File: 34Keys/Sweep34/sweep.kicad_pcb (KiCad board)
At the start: 2 copper layers, 110 x 88.6 mm, 21 parts, among them J1 MJ-4PP-9, SW10 SW_PUSH, SW11 SW_PUSH, SW12 SW_PUSH, SW14 SW_PUSH, SW15 SW_PUSH, SW16 SW_PUSH, SW17 SW_PUSH, SW18 SW_PUSH, SW2 SW_PUSH, SW20 SW_PUSH, SW21 SW_PUSH, SW3 SW_PUSH, SW4 SW_PUSH, SW5 SW_PUSH, SW6 SW_PUSH, SW8 SW_PUSH, SW9 SW_PUSH, U1 ProMicro

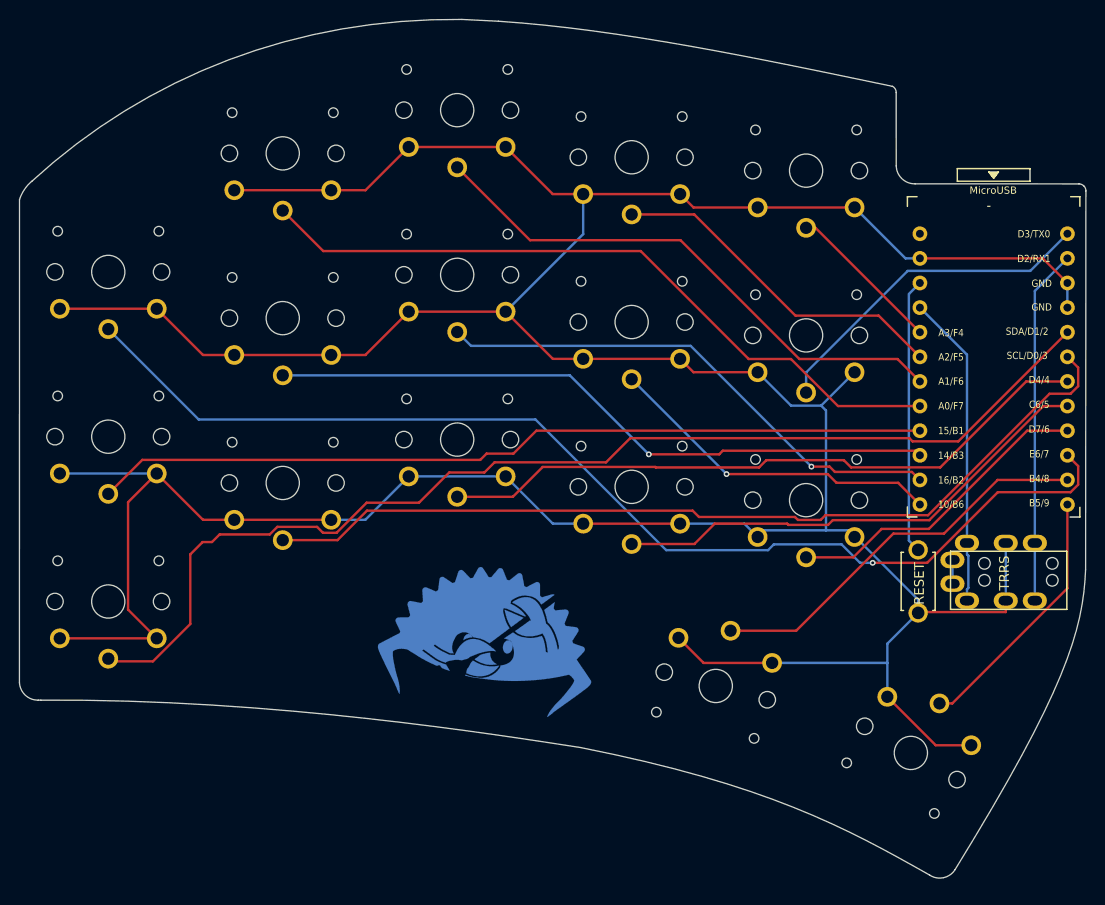
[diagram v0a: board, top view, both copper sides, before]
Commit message: fix promicro footprint, centre ferris move thumbs.
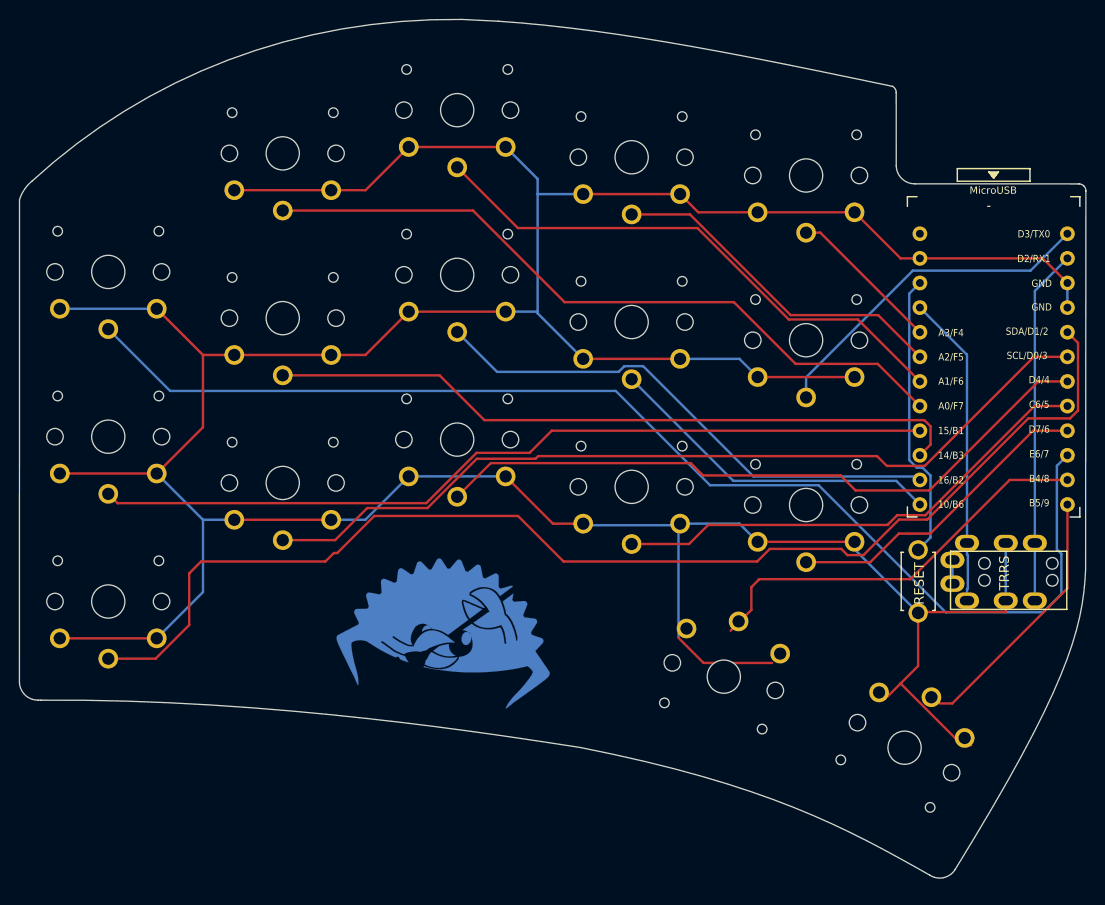
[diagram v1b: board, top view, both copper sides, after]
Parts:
- moved G*** 4.36 mm to (80.1, 80.4)
- moved SW20 1.27 mm to (107.5, 84.1)
- moved SW21 0.85 mm to (126.2, 91.5), turned to 332 degrees
- moved SW12 0.50 mm to (116.0, 49.4)
- moved SW18 0.50 mm to (116.0, 66.4)
- moved SW6 0.50 mm to (116.0, 32.4)
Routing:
- net GND: track 404.5 -> 393.6 mm
- net row3: track 117.4 -> 126.2 mm, vias 1 -> 0
- net SDA: track 118.1 -> 126.7 mm
- net SCL: track 92.9 -> 89.6 mm
- net col5: track 69.5 -> 72.5 mm, vias 1 -> 0
- net row0: track 68.6 -> 70.2 mm
- net Net-(U1-Pad11): track 41.2 -> 42.6 mm
- net reset: track 28.4 -> 29.8 mm
- net col4: track 86.4 -> 87.2 mm
- net Net-(U1-Pad14): track 54.1 -> 54.6 mm, vias 1 -> 0
- net Net-(U1-Pad13): vias 1 -> 0

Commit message: let's get these thumbs something like ferris
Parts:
- moved SW20 1.74 mm to (109.0, 85.1)
- moved SW21 1.72 mm to (127.6, 92.4)
- moved G*** 0.28 mm to (79.8, 80.3)
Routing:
- net GND: track 393.6 -> 396.0 mm
- net Net-(U1-Pad11): track 42.6 -> 41.7 mm
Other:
- board size 110 x 88.6 mm -> 110 x 89.3 mm
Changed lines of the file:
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@@
   )
   (module Kailh:SW_PG1350_reversible_b2 (layer B.Cu)
-    (at 126.16 91.46 332)
+    (at 127.6 92.4 332)
     (descr "Kailh \"Choc\" PG1350 keyswitch, able to be mounted on front or back of PCB")
     (tags kailh,choc)
@@
   )
   (module Kailh:SW_PG1350_reversible_b2 (layer B.Cu)
-    (at 107.51 84.13 345)
+    (at 108.966 85.09 345)
     (descr "Kailh \"Choc\" PG1350 keyswitch, able to be mounted on front or back of PCB")
     (tags kailh,choc)
@@
   )
   (module Kailh:ferris_broom (layer B.Cu)
-    (at 80.07 80.4 171)
+    (at 79.8 80.33 171)
     (fp_text reference G*** (at 0 0 351) (layer B.SilkS) hide
       (effects (font (size 1.524 1.524) (thickness 0.3)) (justify mirror))
@@
   (gr_curve (pts (xy 144.87 34.010455) (xy 144.870889 33.819247) (xy 144.795513 33.637251) (xy 144.655943 33.499545)) (layer Edge.Cuts) (width 0.011328))
   (gr_curve (pts (xy 125.294806 23.859172) (xy 125.294794 23.580455) (xy 125.132917 23.327117) (xy 124.9 23.22)) (layer Edge.Cuts) (width 0.011328))
-  (gr_curve (pts (xy 130.186173 104.869608) (xy 130.675764 104.762323) (xy 131.102064 104.463579) (xy 131.37 104.04)) (layer Edge.Cuts) (width 0.011328))
-  (gr_curve (pts (xy 128.763902 104.611077) (xy 129.184419 104.883795) (xy 129.696582 104.976892) (xy 130.186173 104.869608)) (layer Edge.Cuts) (width 0.011328))
+  (gr_curve (pts (xy 131.55 105.61) (xy 132.039591 105.502715) (xy 132.465891 105.203971) (xy 132.73 104.79)) (layer Edge.Cuts) (width 0.011328))
+  (gr_curve (pts (xy 130.127729 105.351469) (xy 130.548246 105.624187) (xy 131.060409 105.717284) (xy 131.55 105.61)) (layer Edge.Cuts) (width 0.011328))
   (gr_curve (pts (xy 34.833624 84.713423) (xy 34.87005 85.754071) (xy 35.733715 86.573551) (xy 36.77484 86.555327)) (layer Edge.Cuts) (width 0.011328))
-  (gr_curve (pts (xy 128.763902 104.611077) (xy 120.073417 99.705624) (xy 111.98 95.25) (xy 92.71 91.44)) (layer Edge.Cuts) (width 0.011328))
+  (gr_curve (pts (xy 130.127729 105.351469) (xy 120.073417 99.705624) (xy 111.83 95.11) (xy 92.71 91.44)) (layer Edge.Cuts) (width 0.011328))
   (gr_line (start 125.3 31.44) (end 125.294806 23.859172) (layer Edge.Cuts) (width 0.011328))
   (gr_curve (pts (xy 124.9 23.22) (xy 111.07043 20.337524) (xy 96.846186 17.334305) (xy 84.254525 16.504695)) (layer Edge.Cuts) (width 0.011328))
@@
   (gr_curve (pts (xy 80.49 16.32) (xy 63.51 16.12) (xy 48.01 22.1) (xy 36.11 33.02)) (layer Edge.Cuts) (width 0.011328))
   (gr_line (start 144.87 34.010455) (end 144.84 73.04) (layer Edge.Cuts) (width 0.011328))
-  (gr_curve (pts (xy 131.37 104.04) (xy 142.702381 85.610668) (xy 144.590037 79.411298) (xy 144.84 73.04)) (layer Edge.Cuts) (width 0.011328))
+  (gr_curve (pts (xy 132.73 104.79) (xy 144.15 87.83) (xy 144.590037 79.411298) (xy 144.84 73.04)) (layer Edge.Cuts) (width 0.011328))
   (segment (start 142.9614 53.672) (end 139.966 53.672) (width 0.25) (layer F.Cu) (net 1))
   (segment (start 139.966 53.672) (end 128.7186 64.9194) (width 0.25) (layer F.Cu) (net 1))
@@
   (segment (start 49 80.175) (end 39 80.175) (width 0.25) (layer F.Cu) (net 5))
   (segment (start 102.8339 68.5111) (end 103 68.345) (width 0.25) (layer B.Cu) (net 5))
-  (segment (start 102.8339 80.1254) (end 102.8339 68.5111) (width 0.25) (layer B.Cu) (net 5))
   (segment (start 102.8339 68.5111) (end 93.1661 68.5111) (width 0.25) (layer B.Cu) (net 5))
   (segment (start 93.1661 68.5111) (end 93 68.345) (width 0.25) (layer B.Cu) (net 5))
@@
   (segment (start 88.2995 46.6395) (end 88.2995 46.47) (width 0.25) (layer B.Cu) (net 5))
   (segment (start 88.2995 46.47) (end 85 46.47) (width 0.25) (layer B.Cu) (net 5))
-  (segment (start 125.7506 84.8384) (end 124.3799 86.2091) (width 0.25) (layer F.Cu) (net 5))
-  (segment (start 127.56 77.55) (end 127.56 83.029) (width 0.25) (layer F.Cu) (net 5))
-  (segment (start 127.56 83.029) (end 125.7506 84.8384) (width 0.25) (layer F.Cu) (net 5))
-  (segment (start 125.7506 84.8384) (end 132.1213 91.2091) (width 0.25) (layer F.Cu) (net 5))
-  (segment (start 132.1213 91.2091) (end 133.0401 91.2091) (width 0.25) (layer F.Cu) (net 5))
   (segment (start 136.6 77.4653) (end 127.6447 77.4653) (width 0.25) (layer F.Cu) (net 5))
   (segment (start 127.6447 77.4653) (end 127.56 77.55) (width 0.25) (layer F.Cu) (net 5))
@@
   (segment (start 75 63.47) (end 70.525 67.945) (width 0.25) (layer B.Cu) (net 5))
   (segment (start 70.525 67.945) (end 67 67.945) (width 0.25) (layer B.Cu) (net 5))
-  (segment (start 112.4931 82.7136) (end 105.4221 82.7136) (width 0.25) (layer F.Cu) (net 5))
-  (segment (start 105.4221 82.7136) (end 102.8339 80.1254) (width 0.25) (layer F.Cu) (net 5))
   (segment (start 142.9614 43.512) (end 140.4214 40.972) (width 0.25) (layer F.Cu) (net 5))
   (segment (start 140.4214 40.972) (end 127.7414 40.972) (width 0.25) (layer F.Cu) (net 5))
@@
   (segment (start 136.6 76.29) (end 136.6 77.4653) (width 0.25) (layer F.Cu) (net 5))
   (segment (start 136.6 76.29) (end 136.6 70.34) (width 0.25) (layer B.Cu) (net 5))
+  (segment (start 103 78.501504) (end 103.663883 79.165387) (width 0.25) (layer B.Cu) (net 5))
+  (segment (start 103 68.345) (end 103 78.501504) (width 0.25) (layer B.Cu) (net 5))
+  (segment (start 127.56 84.106695) (end 124.969254 86.697441) (width 0.25) (layer F.Cu) (net 5))
+  (segment (start 127.56 77.55) (end 127.56 84.106695) (width 0.25) (layer F.Cu) (net 5))
+  (segment (start 129.66397 91.392157) (end 133.79873 91.392157) (width 0.25) (layer F.Cu) (net 5))
+  (segment (start 124.969254 86.697441) (end 129.66397 91.392157) (width 0.25) (layer F.Cu) (net 5))
+  (segment (start 107.762073 82.633577) (end 105.173883 80.045387) (width 0.25) (layer B.Cu) (net 5))
+  (segment (start 114.833142 82.633577) (end 107.762073 82.633577) (width 0.25) (layer B.Cu) (net 5))
+  (segment (start 104.293883 79.165387) (end 105.173883 80.045387) (width 0.25) (layer B.Cu) (net 5))
+  (segment (start 103.663883 79.165387) (end 104.293883 79.165387) (width 0.25) (layer B.Cu) (net 5))
   (segment (start 132.6 69.1647) (end 132.6 50.9106) (width 0.25) (layer B.Cu) (net 6))
   (segment (start 132.6 50.9106) (end 127.7414 46.052) (width 0.25) (layer B.Cu) (net 6))
@@
   (segment (start 108.4899 63.9299) (end 98 53.44) (width 0.25) (layer B.Cu) (net 21))
   (segment (start 142.9614 66.372) (end 142.9614 75.0149) (width 0.25) (layer F.Cu) (net 22))
-  (segment (start 142.9614 75.0149) (end 131.0858 86.8905) (width 0.25) (layer F.Cu) (net 22))
-  (segment (start 131.0858 86.8905) (end 129.76 86.8905) (width 0.25) (layer F.Cu) (net 22))
-  (segment (start 137.0102 63.832) (end 142.9614 63.832) (width 0.25) (layer F.Cu) (net 23))
-  (segment (start 127.4086 73.4336) (end 137.0102 63.832) (width 0.25) (layer F.Cu) (net 23))
-  (segment (start 110.35 77.24807) (end 108.207032 79.391038) (width 0.25) (layer F.Cu) (net 23))
+  (segment (start 142.9614 75.0149) (end 136.88815 81.08815) (width 0.25) (layer F.Cu) (net 22))
+  (segment (start 136.472341 81.08815) (end 130.369882 87.190609) (width 0.25) (layer F.Cu) (net 22))
+  (segment (start 136.88815 81.08815) (end 136.472341 81.08815) (width 0.25) (layer F.Cu) (net 22))
+  (segment (start 110.35 74.9) (end 110.35 79.114006) (width 0.25) (layer F.Cu) (net 23))
+  (segment (start 110.35 79.114006) (end 110.547032 79.311038) (width 0.25) (layer F.Cu) (net 23))
+  (segment (start 142.9614 63.832) (end 137.0102 63.832) (width 0.25) (layer F.Cu) (net 23))
   (segment (start 111.125 74.125) (end 110.35 74.9) (width 0.25) (layer F.Cu) (net 23))
+  (segment (start 137.0102 63.832) (end 126.7672 74.075) (width 0.25) (layer F.Cu) (net 23))
+  (segment (start 126.7672 74.075) (end 111.125 74.075) (width 0.25) (layer F.Cu) (net 23))
   (segment (start 111.125 74.075) (end 111.125 74.125) (width 0.25) (layer F.Cu) (net 23))
-  (segment (start 111.125 74.075) (end 123.65 74.075) (width 0.25) (layer F.Cu) (net 23))
-  (segment (start 110.35 74.9) (end 110.35 77.24807) (width 0.25) (layer F.Cu) (net 23))
-  (segment (start 126.7672 74.075) (end 126.8711 73.9711) (width 0.25) (layer F.Cu) (net 23))
-  (segment (start 123.65 74.075) (end 126.7672 74.075) (width 0.25) (layer F.Cu) (net 23))
-  (segment (start 126.8711 73.9711) (end 127.4086 73.4336) (width 0.25) (layer F.Cu) (net 23))
 )

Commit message: curve changes
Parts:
- moved G*** 2.18 mm to (81.0, 82.2)
- moved SW21 1.02 mm to (128.5, 92.8), turned to 330 degrees
- moved SW20 0.82 mm to (109.8, 85.0)
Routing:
- net Net-(U1-Pad11): track 41.7 -> 38.3 mm
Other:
- board size 110 x 89.3 mm -> 110 x 88.3 mm
